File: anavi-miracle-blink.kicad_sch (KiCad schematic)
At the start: 11 parts, among them J4 Conn_01x04_Female, J7 Screw_Terminal_01x03, SW1 SW_DIP_x01, U1 MOUDLE-SEEEDUINO-XIAO-ESP32C3, U2 74LVC1G17W5-7

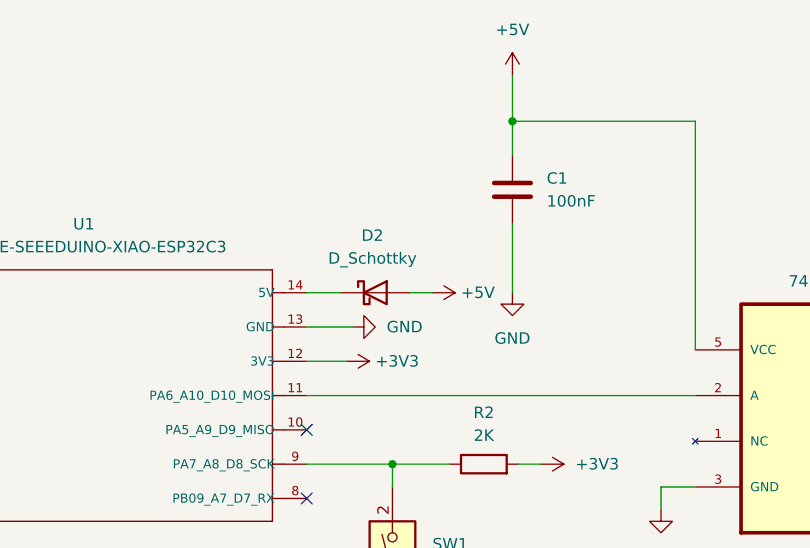
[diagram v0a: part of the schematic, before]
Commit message: Rev 1.1: Remove Schottky diode
Remove Schottky diode to allow using the USB-C as power source for
NeoPixel LEDs. The Schottky diode can still be added externally in
the use case of external 5V power supply.

Signed-off-by: Leon Anavi <leon@anavi.org>
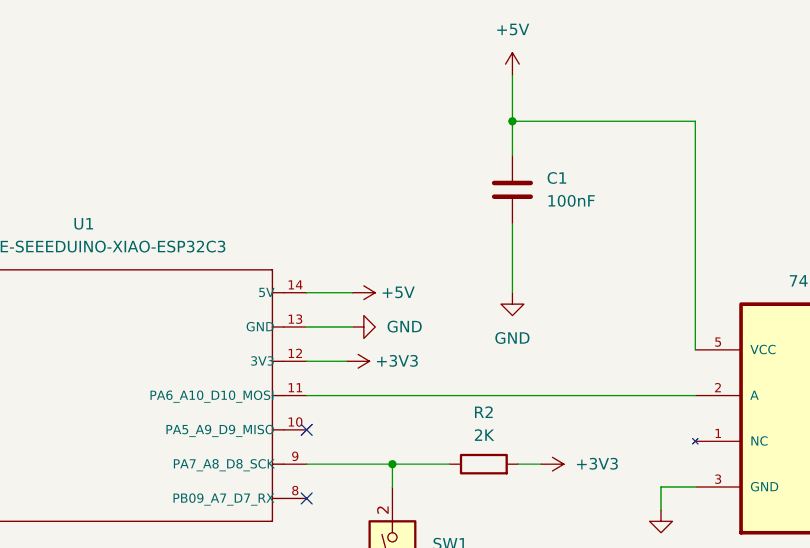
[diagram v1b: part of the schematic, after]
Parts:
- removed D2: D_Schottky, Diode_SMD:D_SMA, symbol Device:D_Schottky
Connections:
- net +5V: now also U1.14 (5V)
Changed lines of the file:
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@@
+	(wire
+		(pts
+			(xy 151.13 64.77) (xy 156.21 64.77)
+		)
+		(stroke
+			(width 0)
+			(type default)
+		)
+	)
 	(wire
 		(pts
@@
 	(wire
 		(pts
-			(xy 162.56 64.77) (xy 165.1 64.77)
-		)
-		(stroke
-			(width 0)
-			(type default)
-		)
-	)
-	(wire
-		(pts
 			(xy 96.52 76.2) (xy 101.6 76.2)
-		)
-		(stroke
-			(width 0)
-			(type default)
-		)
-	)
-	(wire
-		(pts
-			(xy 151.13 64.77) (xy 154.94 64.77)
 		)
 		(stroke
@@
 	(symbol
 		(lib_id "power:+5V")
-		(at 165.1 64.77 270)
+		(at 156.21 64.77 270)
 		(unit 1)
 		(exclude_from_sim no)
@@
 		(fields_autoplaced yes)
 		(property "Reference" "#PWR010"
-			(at 161.29 64.77 0)
+			(at 152.4 64.77 0)
 			(effects
 				(font
@@
 		)
 		(property "Value" "+5V"
-			(at 168.275 64.7699 90)
+			(at 159.385 64.7699 90)
 			(effects
 				(font
@@
 		)
 		(property "Footprint" ""
-			(at 165.1 64.77 0)
+			(at 156.21 64.77 0)
 			(effects
 				(font
@@
 		)
 		(property "Datasheet" ""
-			(at 165.1 64.77 0)
+			(at 156.21 64.77 0)
 			(effects
 				(font
@@
 		)
 		(property "Description" ""
-			(at 165.1 64.77 0)
+			(at 156.21 64.77 0)
 			(effects
 				(font
@@
 					(unit 1)
 				)
-			)
-		)
-	)
-	(symbol
-		(lib_id "Device:D_Schottky")
-		(at 158.75 64.77 0)
-		(unit 1)
-		(exclude_from_sim no)
-		(in_bom yes)
-		(on_board yes)
-		(dnp no)
-		(fields_autoplaced yes)
-		(property "Reference" "D2"
-			(at 158.4325 58.42 0)
-			(effects
-				(font
-					(size 1.27 1.27)
-				)
-			)
-		)
-		(property "Value" "D_Schottky"
-			(at 158.4325 60.96 0)
-			(effects
-				(font
-					(size 1.27 1.27)
-				)
-			)
-		)
-		(property "Footprint" "Diode_SMD:D_SMA"
-			(at 158.75 64.77 0)
-			(effects
-				(font
-					(size 1.27 1.27)
-				)
-				(hide yes)
-			)
-		)
-		(property "Datasheet" "~"
-			(at 158.75 64.77 0)
-			(effects
-				(font
-					(size 1.27 1.27)
-				)
-				(hide yes)
-			)
-		)
-		(property "Description" "Schottky diode"
-			(at 158.75 64.77 0)
-			(effects
-				(font
-					(size 1.27 1.27)
-				)
-				(hide yes)
-			)
-		)
-		(pin "1"
-		)
-		(pin "2"
-		)
-		(instances
-			(project ""
-				(path "/2ff006f4-2a61-440d-9643-0ab2f7506f70"
-					(reference "D2")
-					(unit 1)
-				)
